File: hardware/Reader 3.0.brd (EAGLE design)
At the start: 55.9 x 58.4 mm, 14 parts, among them J1 54601-908WPLFW/MODEL, U1 ESP32-DEVKITC-32DHEADERS_ONLY

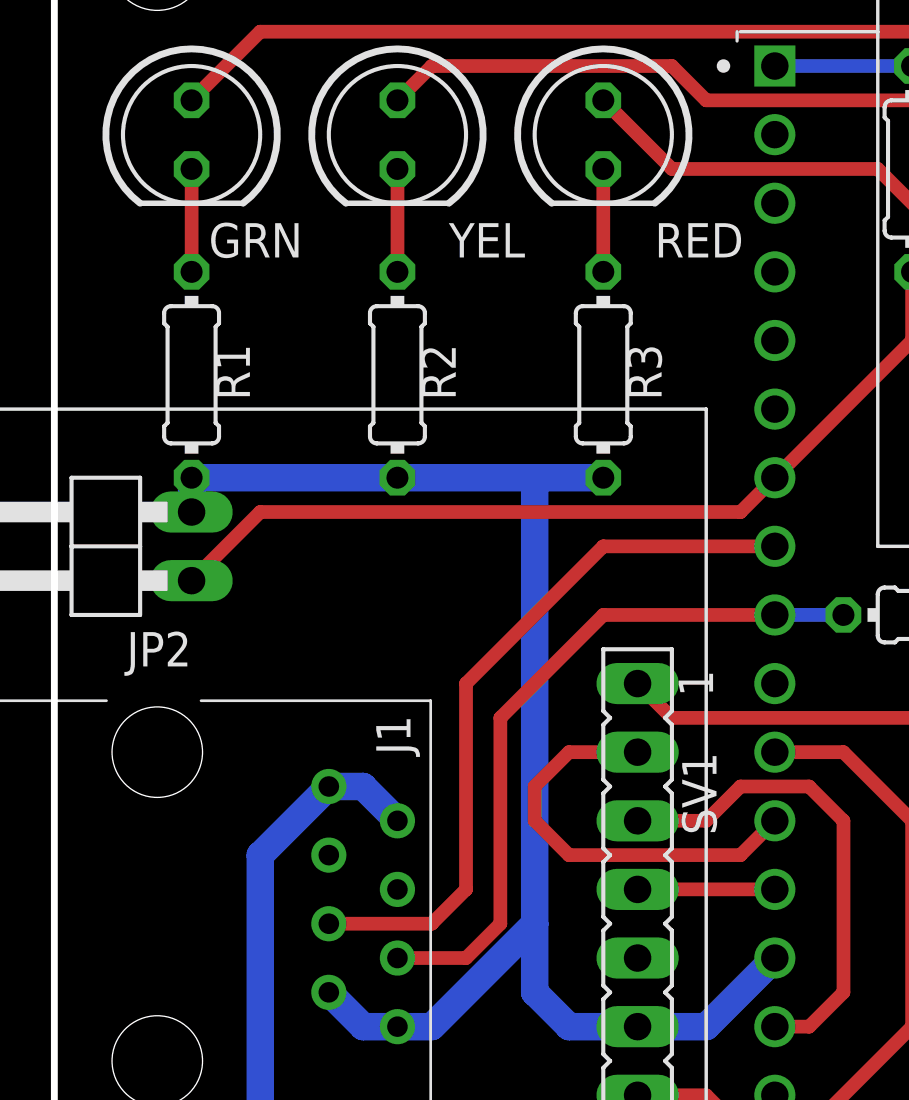
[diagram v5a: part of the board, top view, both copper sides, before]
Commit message: adjust LED resistor positions
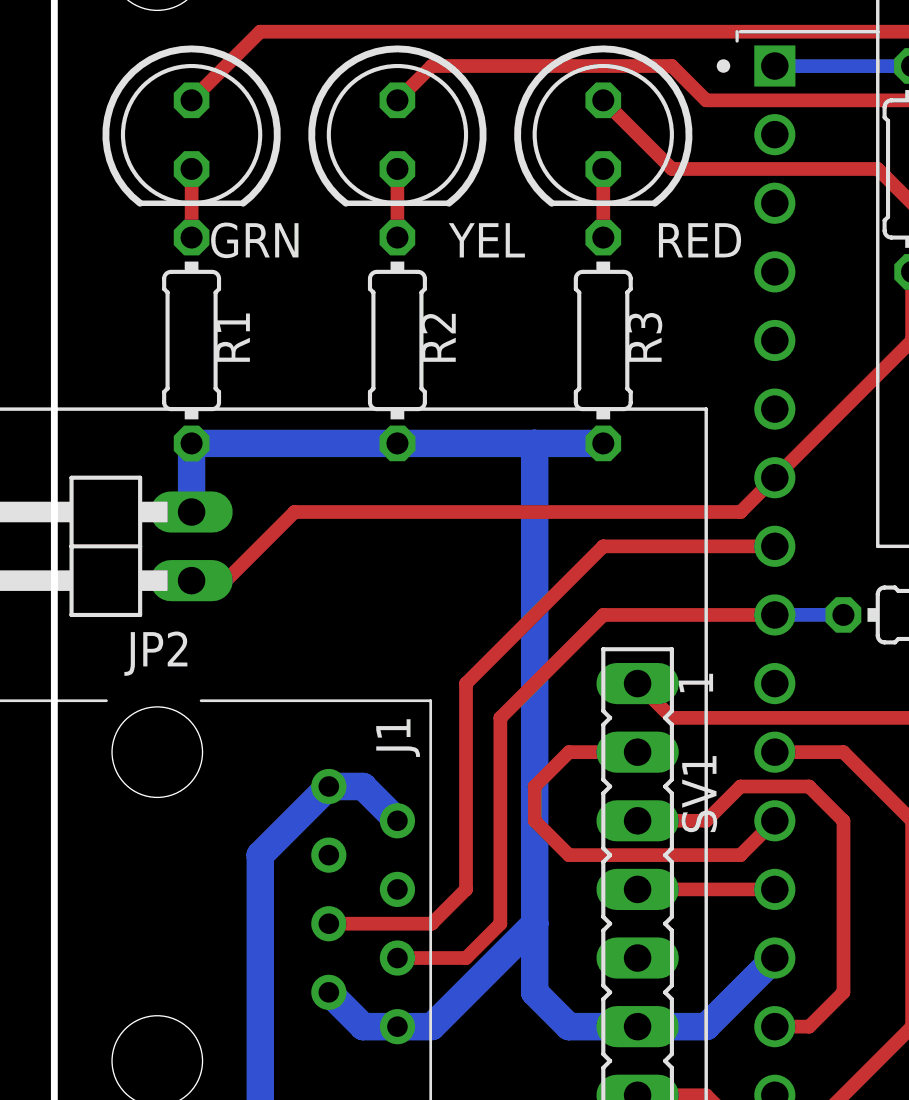
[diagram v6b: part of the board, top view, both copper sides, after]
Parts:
- moved R1 1.27 mm to (5.08, 40.6)
- moved R2 1.27 mm to (12.7, 40.6)
- moved R3 1.27 mm to (20.3, 40.6)
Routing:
- net GND: track 55.8 -> 58.3 mm
- net N$6: track 3.81 -> 2.54 mm
- net N$5: track 3.81 -> 2.54 mm
- net N$4: track 3.81 -> 2.54 mm
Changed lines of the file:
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@@
 <attribute name="VALUE" x="3.2766" y="45.0596" size="1.27" layer="27" ratio="10" rot="R270"/>
 </element>
-<element name="R1" library="mcp" library_urn="urn:adsk.eagle:library:9418757" package="0204/7" package3d_urn="urn:adsk.eagle:package:23498/2" value="330" x="5.08" y="39.37" smashed="yes" rot="R270">
-<attribute name="NAME" x="5.969" y="40.513" size="1.27" layer="25" ratio="10" rot="R270"/>
-<attribute name="VALUE" x="2.921" y="40.513" size="1.27" layer="27" ratio="10" rot="R270"/>
+<element name="R1" library="mcp" library_urn="urn:adsk.eagle:library:9418757" package="0204/7" package3d_urn="urn:adsk.eagle:package:23498/2" value="330" x="5.08" y="40.64" smashed="yes" rot="R270">
+<attribute name="NAME" x="5.969" y="41.783" size="1.27" layer="25" ratio="10" rot="R270"/>
+<attribute name="VALUE" x="2.921" y="41.783" size="1.27" layer="27" ratio="10" rot="R270"/>
 </element>
-<element name="R2" library="mcp" library_urn="urn:adsk.eagle:library:9418757" package="0204/7" package3d_urn="urn:adsk.eagle:package:23498/2" value="330" x="12.7" y="39.37" smashed="yes" rot="R270">
-<attribute name="NAME" x="13.589" y="40.513" size="1.27" layer="25" ratio="10" rot="R270"/>
-<attribute name="VALUE" x="10.541" y="40.513" size="1.27" layer="27" ratio="10" rot="R270"/>
+<element name="R2" library="mcp" library_urn="urn:adsk.eagle:library:9418757" package="0204/7" package3d_urn="urn:adsk.eagle:package:23498/2" value="330" x="12.7" y="40.64" smashed="yes" rot="R270">
+<attribute name="NAME" x="13.589" y="41.783" size="1.27" layer="25" ratio="10" rot="R270"/>
+<attribute name="VALUE" x="10.541" y="41.783" size="1.27" layer="27" ratio="10" rot="R270"/>
 </element>
-<element name="R3" library="mcp" library_urn="urn:adsk.eagle:library:9418757" package="0204/7" package3d_urn="urn:adsk.eagle:package:23498/2" value="330" x="20.32" y="39.37" smashed="yes" rot="R270">
-<attribute name="NAME" x="21.209" y="40.513" size="1.27" layer="25" ratio="10" rot="R270"/>
-<attribute name="VALUE" x="18.161" y="40.513" size="1.27" layer="27" ratio="10" rot="R270"/>
+<element name="R3" library="mcp" library_urn="urn:adsk.eagle:library:9418757" package="0204/7" package3d_urn="urn:adsk.eagle:package:23498/2" value="330" x="20.32" y="40.64" smashed="yes" rot="R270">
+<attribute name="NAME" x="21.209" y="41.783" size="1.27" layer="25" ratio="10" rot="R270"/>
+<attribute name="VALUE" x="18.161" y="41.783" size="1.27" layer="27" ratio="10" rot="R270"/>
 </element>
 <element name="R4" library="mcp" library_urn="urn:adsk.eagle:library:9418757" package="0204/7" package3d_urn="urn:adsk.eagle:package:23498/2" value="10k" x="31.75" y="46.99" smashed="yes" rot="R270">
@@
 <wire x1="21.59" y1="15.24" x2="24.13" y2="15.24" width="1.016" layer="16"/>
 <wire x1="24.13" y1="15.24" x2="26.67" y2="17.78" width="1.016" layer="16"/>
-<wire x1="20.32" y1="35.56" x2="17.78" y2="35.56" width="1.016" layer="16"/>
-<wire x1="17.78" y1="35.56" x2="12.7" y2="35.56" width="1.016" layer="16"/>
-<wire x1="12.7" y1="35.56" x2="5.08" y2="35.56" width="1.016" layer="16"/>
+<wire x1="20.32" y1="36.83" x2="17.78" y2="36.83" width="1.016" layer="16"/>
+<wire x1="17.78" y1="36.83" x2="12.7" y2="36.83" width="1.016" layer="16"/>
+<wire x1="12.7" y1="36.83" x2="5.08" y2="36.83" width="1.016" layer="16"/>
 <contactref element="J1" pad="8"/>
 <contactref element="J1" pad="4"/>
@@
 <wire x1="12.7" y1="15.24" x2="11.43" y2="15.24" width="1.016" layer="16"/>
 <wire x1="11.43" y1="15.24" x2="10.16" y2="16.51" width="1.016" layer="16"/>
-<wire x1="17.78" y1="19.05" x2="17.78" y2="35.56" width="1.016" layer="16"/>
+<wire x1="17.78" y1="19.05" x2="17.78" y2="36.83" width="1.016" layer="16"/>
 <wire x1="17.78" y1="19.05" x2="17.78" y2="16.51" width="1.016" layer="16"/>
 <wire x1="17.78" y1="16.51" x2="19.05" y2="15.24" width="1.016" layer="16"/>
 <wire x1="19.05" y1="15.24" x2="21.59" y2="15.24" width="1.016" layer="16"/>
 <contactref element="JP2" pad="2"/>
-<wire x1="5.08" y1="34.29" x2="5.08" y2="35.56" width="1.016" layer="16"/>
+<wire x1="5.08" y1="34.29" x2="5.08" y2="36.83" width="1.016" layer="16"/>
 <wire x1="52.07" y1="35.56" x2="52.07" y2="50.8" width="0" layer="19" extent="1-1"/>
 <wire x1="26.67" y1="17.78" x2="52.07" y2="35.56" width="0" layer="19" extent="1-1"/>
@@
 <contactref element="GRN" pad="K"/>
 <contactref element="R1" pad="1"/>
-<wire x1="5.08" y1="43.18" x2="5.08" y2="46.99" width="0.508" layer="1"/>
+<wire x1="5.08" y1="44.45" x2="5.08" y2="46.99" width="0.508" layer="1"/>
 </signal>
 <signal name="N$5">
 <contactref element="YEL" pad="K"/>
 <contactref element="R2" pad="1"/>
-<wire x1="12.7" y1="43.18" x2="12.7" y2="46.99" width="0.508" layer="1"/>
+<wire x1="12.7" y1="44.45" x2="12.7" y2="46.99" width="0.508" layer="1"/>
 </signal>
 <signal name="N$6">
 <contactref element="RED" pad="K"/>
 <contactref element="R3" pad="1"/>
-<wire x1="20.32" y1="43.18" x2="20.32" y2="46.99" width="0.508" layer="1"/>
+<wire x1="20.32" y1="44.45" x2="20.32" y2="46.99" width="0.508" layer="1"/>
 </signal>
 <signal name="POW_SW">
@@
 <wire x1="31.75" y1="40.64" x2="31.75" y2="43.18" width="0.508" layer="1"/>
 <contactref element="JP2" pad="1"/>
-<wire x1="5.08" y1="31.75" x2="7.62" y2="34.29" width="0.508" layer="1"/>
+<wire x1="8.89" y1="34.29" x2="6.35" y2="31.75" width="0.508" layer="1"/>
+<wire x1="5.08" y1="31.75" x2="6.35" y2="31.75" width="0.508" layer="1"/>
 <wire x1="25.4" y1="34.29" x2="26.67" y2="35.56" width="0.508" layer="1"/>
-<wire x1="7.62" y1="34.29" x2="25.4" y2="34.29" width="0.508" layer="1"/>
+<wire x1="8.89" y1="34.29" x2="25.4" y2="34.29" width="0.508" layer="1"/>
 </signal>
 <signal name="RELAY_OUT">

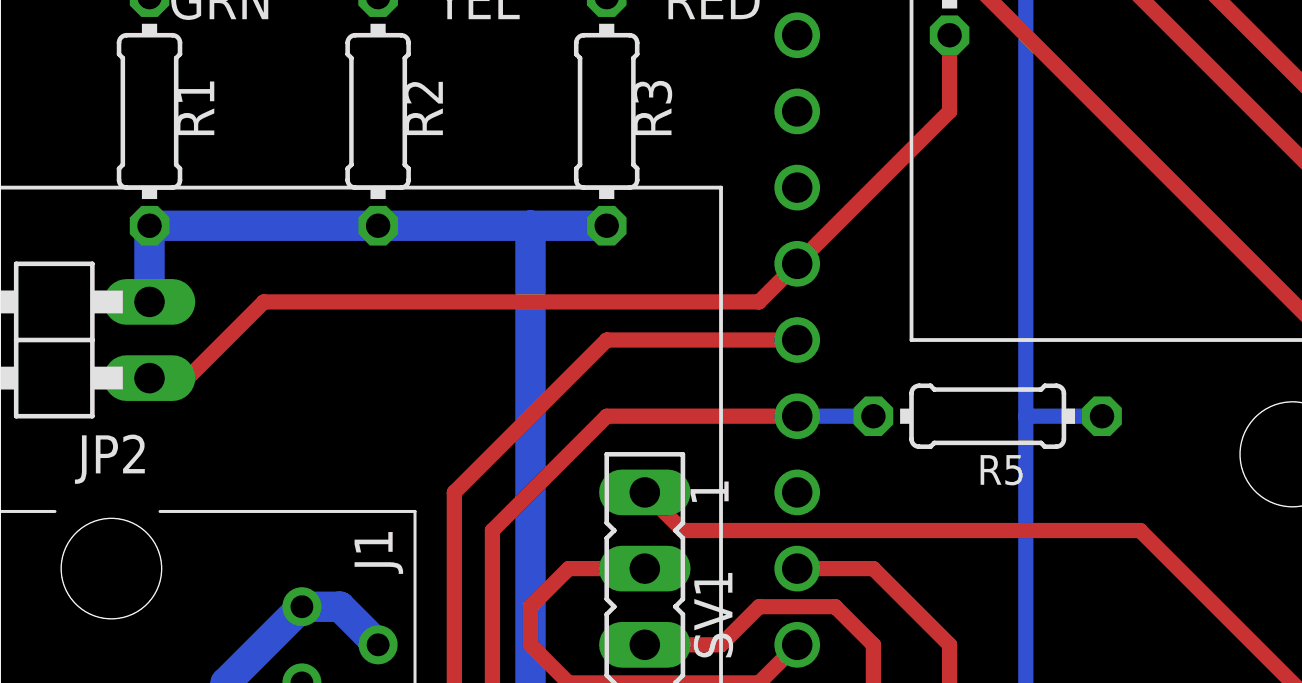
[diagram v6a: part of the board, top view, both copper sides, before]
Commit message: fix current input wiring   * ADC2 on IO25 is not usable when WiFi is active.   * switch to ADC1 on IO32   * add capacitor to input   * remove pullup resistor
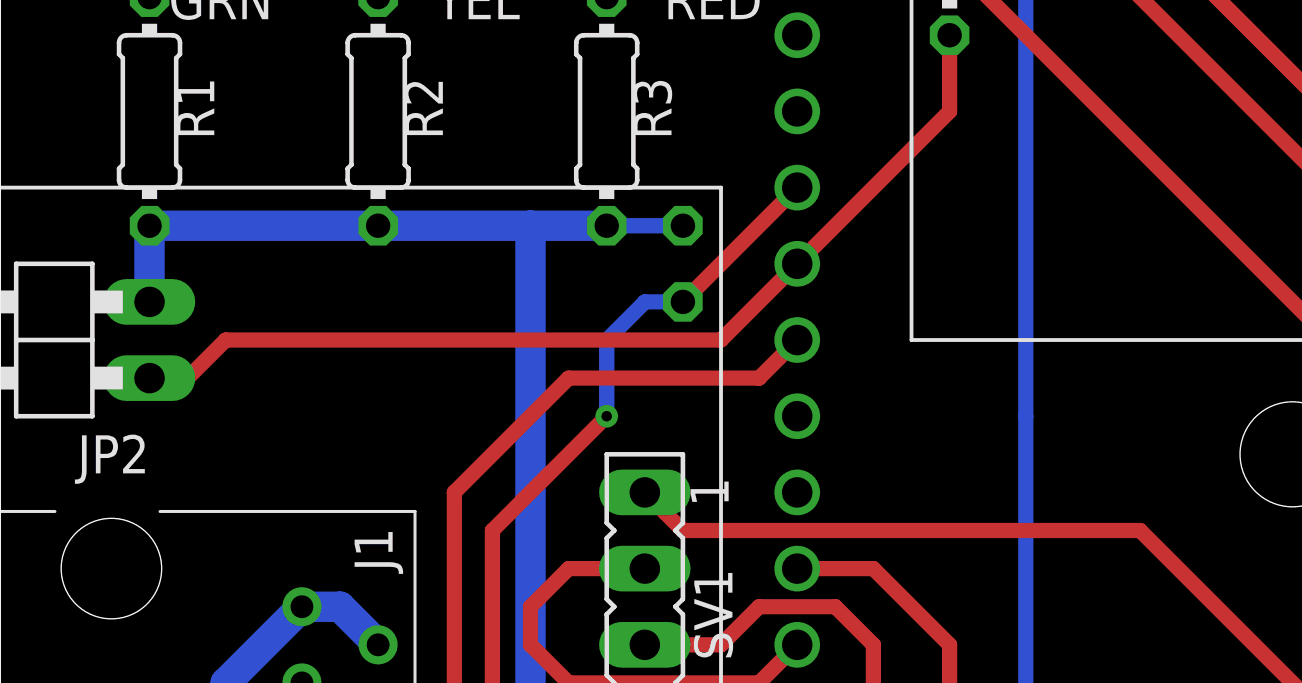
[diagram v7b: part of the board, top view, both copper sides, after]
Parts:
- removed R5: 10k, mcp:0204/7
- added C1: (no value), rcl:C025-025X050
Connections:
- new net N$8: U1.5
- net +3V3: no longer R5.1
- net CURRENT_IN: now also C1.1, U1.6; no longer R5.2, U1.9
- net GND: now also C1.2
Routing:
- net +3V3: track 81.2 -> 78.6 mm
- net GND: track 58.3 -> 60.8 mm
- net CURRENT_IN: track 26.2 -> 28.3 mm, vias 0 -> 1
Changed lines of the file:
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@@
 <attribute name="VALUE" x="5.08" y="37.465" size="1.27" layer="27" rot="R180"/>
 </element>
-<element name="R5" library="mcp" library_urn="urn:adsk.eagle:library:9418757" package="0204/7" package3d_urn="urn:adsk.eagle:package:23498/2" value="10k" x="33.02" y="30.48" smashed="yes" rot="R180">
-<attribute name="NAME" x="34.29" y="29.1846" size="0.9906" layer="25" ratio="10" rot="R180"/>
-<attribute name="VALUE" x="34.6456" y="30.9626" size="0.9906" layer="27" ratio="10" rot="R180"/>
+<element name="C1" library="rcl" library_urn="urn:adsk.eagle:library:334" package="C025-025X050" package3d_urn="urn:adsk.eagle:package:23629/2" value="" x="22.86" y="35.56" smashed="yes" rot="MR90">
+<attribute name="NAME" x="24.384" y="33.274" size="1.27" layer="26" ratio="10" rot="MR90"/>
+<attribute name="SPICEPREFIX" value="C" x="22.86" y="35.56" size="1.778" layer="28" rot="MR90" display="off"/>
+<attribute name="VALUE" x="20.066" y="33.274" size="1.27" layer="28" ratio="10" rot="MR90"/>
 </element>
 </elements>
@@
 <contactref element="JP2" pad="2"/>
 <wire x1="5.08" y1="34.29" x2="5.08" y2="36.83" width="1.016" layer="16"/>
+<contactref element="C1" pad="2"/>
+<wire x1="20.32" y1="36.83" x2="22.86" y2="36.83" width="0.508" layer="16"/>
 <wire x1="52.07" y1="35.56" x2="52.07" y2="50.8" width="0" layer="19" extent="1-1"/>
-<wire x1="26.67" y1="17.78" x2="52.07" y2="35.56" width="0" layer="19" extent="1-1"/>
+<wire x1="22.86" y1="36.83" x2="52.07" y2="35.56" width="0" layer="19" extent="1-1"/>
 </signal>
 <signal name="+3V3">
@@
 <wire x1="40.64" y1="5.08" x2="41.91" y2="6.35" width="0.508" layer="16"/>
 <wire x1="41.91" y1="6.35" x2="41.91" y2="11.43" width="0.508" layer="16"/>
-<contactref element="R5" pad="1"/>
-<wire x1="36.83" y1="30.48" x2="34.29" y2="30.48" width="0.508" layer="16"/>
 </signal>
 <signal name="N$1">
@@
 <wire x1="31.75" y1="40.64" x2="31.75" y2="43.18" width="0.508" layer="1"/>
 <contactref element="JP2" pad="1"/>
-<wire x1="8.89" y1="34.29" x2="6.35" y2="31.75" width="0.508" layer="1"/>
+<wire x1="7.62" y1="33.02" x2="6.35" y2="31.75" width="0.508" layer="1"/>
 <wire x1="5.08" y1="31.75" x2="6.35" y2="31.75" width="0.508" layer="1"/>
-<wire x1="25.4" y1="34.29" x2="26.67" y2="35.56" width="0.508" layer="1"/>
-<wire x1="8.89" y1="34.29" x2="25.4" y2="34.29" width="0.508" layer="1"/>
+<wire x1="24.13" y1="33.02" x2="26.67" y2="35.56" width="0.508" layer="1"/>
+<wire x1="7.62" y1="33.02" x2="24.13" y2="33.02" width="0.508" layer="1"/>
 </signal>
 <signal name="RELAY_OUT">
@@
 <wire x1="15.24" y1="20.32" x2="15.24" y2="27.94" width="0.508" layer="1"/>
 <contactref element="U1" pad="8"/>
-<wire x1="15.24" y1="27.94" x2="20.32" y2="33.02" width="0.508" layer="1"/>
-<wire x1="20.32" y1="33.02" x2="26.67" y2="33.02" width="0.508" layer="1"/>
+<wire x1="15.24" y1="27.94" x2="19.05" y2="31.75" width="0.508" layer="1"/>
+<wire x1="25.4" y1="31.75" x2="26.67" y2="33.02" width="0.508" layer="1"/>
+<wire x1="25.4" y1="31.75" x2="19.05" y2="31.75" width="0.508" layer="1"/>
 </signal>
 <signal name="IO2">
@@
 </signal>
 <signal name="CURRENT_IN">
-<contactref element="U1" pad="9"/>
 <contactref element="J1" pad="7"/>
-<wire x1="12.7" y1="17.78" x2="15.24" y2="17.78" width="0.508" layer="1"/>
+<contactref element="U1" pad="6"/>
+<contactref element="C1" pad="1"/>
 <wire x1="15.24" y1="17.78" x2="16.51" y2="19.05" width="0.508" layer="1"/>
 <wire x1="16.51" y1="19.05" x2="16.51" y2="26.67" width="0.508" layer="1"/>
 <wire x1="16.51" y1="26.67" x2="20.32" y2="30.48" width="0.508" layer="1"/>
-<wire x1="20.32" y1="30.48" x2="26.67" y2="30.48" width="0.508" layer="1"/>
-<contactref element="R5" pad="2"/>
-<wire x1="26.67" y1="30.48" x2="29.21" y2="30.48" width="0.508" layer="16"/>
+<via x="20.32" y="30.48" extent="1-16" drill="0.35"/>
+<wire x1="20.32" y1="30.48" x2="20.32" y2="33.02" width="0.508" layer="16"/>
+<wire x1="20.32" y1="33.02" x2="21.59" y2="34.29" width="0.508" layer="16"/>
+<wire x1="21.59" y1="34.29" x2="22.86" y2="34.29" width="0.508" layer="16"/>
+<wire x1="12.7" y1="17.78" x2="15.24" y2="17.78" width="0.508" layer="1"/>
+<wire x1="22.86" y1="34.29" x2="26.67" y2="38.1" width="0.508" layer="1"/>
+</signal>
+<signal name="N$8">
+<contactref element="U1" pad="5"/>
 </signal>
 </signals>
